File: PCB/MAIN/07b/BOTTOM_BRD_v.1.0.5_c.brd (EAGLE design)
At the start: 99.1 x 85.8 mm, 66 parts, among them Q1 SS8050, Q2 SS8050, Q4 TIP122, SW1 CS12ANW03, U1 ESP32-WROOM-32D, U2 L293D, U3 AP2112K-3.3, U4 CE8301

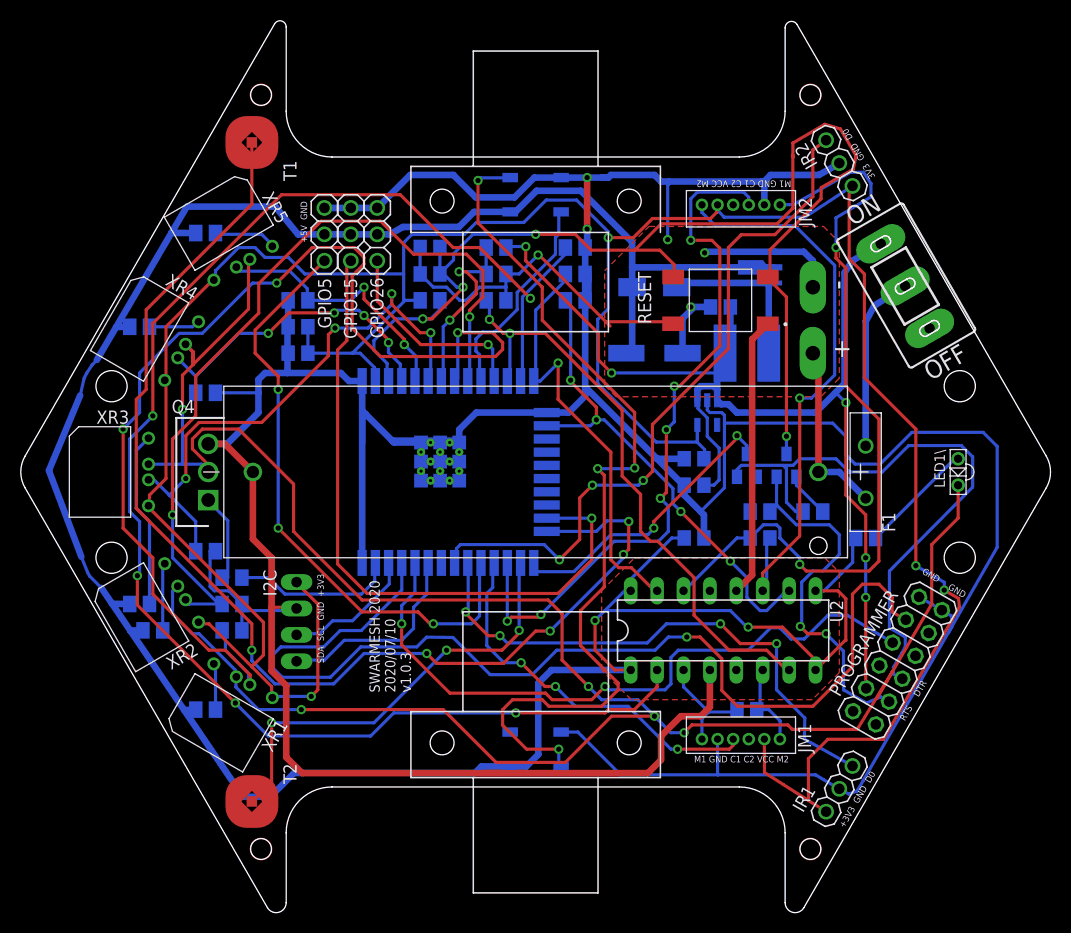
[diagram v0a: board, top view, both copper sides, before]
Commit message: Update pcb v.1.0.3
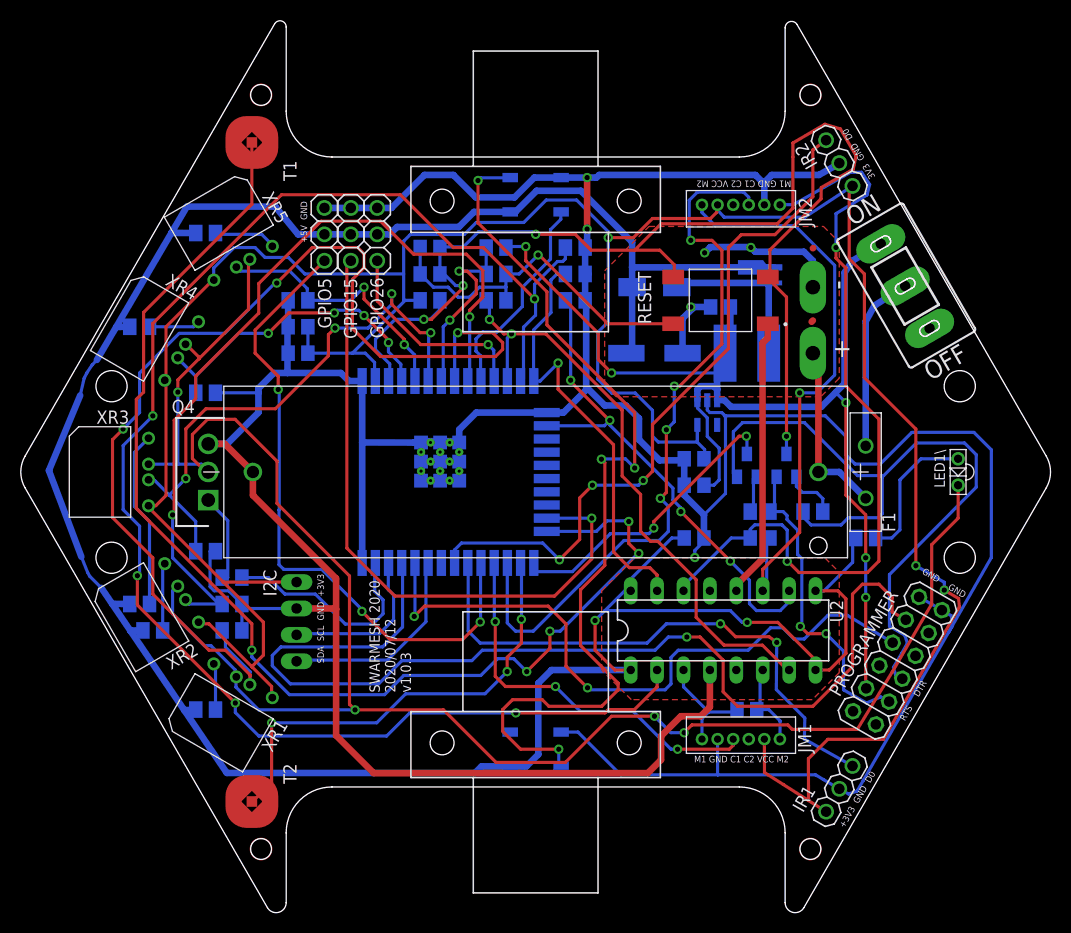
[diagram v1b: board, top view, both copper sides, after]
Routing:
- net N$8: track 206.4 -> 177.6 mm, vias 5 -> 4
- net GND: track 512.5 -> 495.5 mm, vias 6 -> 7
- net DTR: track 57.8 -> 71.5 mm
- net +3V3: track 282.1 -> 275.5 mm, vias 4 -> 3
- net RTS: track 36.5 -> 30.9 mm
- net IRTX: track 15.7 -> 21.1 mm
- net IO5: track 58.0 -> 61.9 mm
- net TOUCH1: track 113.6 -> 116.9 mm
- net N$14: track 11.1 -> 13.9 mm
- net SCL: track 13.0 -> 15.6 mm
- net +5V: track 254.9 -> 252.6 mm
- net IO15: track 65.0 -> 63.0 mm
- net IO13: track 46.6 -> 48.3 mm
- net TOUCH2: track 42.6 -> 44.1 mm
- net M2A: track 74.7 -> 76.1 mm
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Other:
- board text added: "SWARMESH 2020 2020/07/12 v1.0.3"
- board text removed: "SWARMESH 2020 2020/07/10 v1.0.3"

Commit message: Update BOTTOM_BRD_v.1.0.5_c.brd
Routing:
- net GND: track 495.5 -> 484.1 mm, vias 7 -> 5
- net EN: track 114.5 -> 124.3 mm
- net IR2: track 67.9 -> 75.1 mm, vias 3 -> 6
- net VCC: track 110.5 -> 116.9 mm
- net +5V: track 252.6 -> 257.0 mm

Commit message: Update BOTTOM_BRD_v.1.0.5_c.brd
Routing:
- net M2A: track 76.2 -> 103.2 mm, vias 2 -> 0
- net +5V: track 257.0 -> 278.7 mm, vias 2 -> 0
- net GND: track 484.1 -> 505.6 mm, vias 5 -> 4
- net M2B: track 56.3 -> 62.9 mm, vias 1 -> 2
- net VCC: track 116.9 -> 122.6 mm
- net RTS: track 30.9 -> 36.0 mm, vias 2 -> 4
- net IR1: track 53.9 -> 51.4 mm, vias 2 -> 0
- net IO27: track 57.6 -> 59.9 mm
- net +3V3: track 275.1 -> 273.3 mm
- net LEDS: track 20.6 -> 22.5 mm
- net RXD: track 100.0 -> 98.4 mm
- net IO13: track 48.8 -> 50.4 mm
- net N$1: track 17.3 -> 18.6 mm
- net N$9: track 87.9 -> 89.1 mm
- net IO12: track 42.1 -> 41.2 mm
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
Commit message: Update BOTTOM_BRD_v.1.0.5_c.brd
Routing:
- net EN: track 124.3 -> 99.2 mm
- net M2B: track 62.9 -> 58.1 mm, vias 2 -> 0
- net N$1: track 18.6 -> 17.3 mm
- net +3V3: track 273.3 -> 274.5 mm
